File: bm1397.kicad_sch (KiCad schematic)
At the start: 68 parts, among them IC1 BM1397_mode1, J3 Conn_01x05, U2 LN1134A182MR-G, U3 SN74LVC1T45DBVR, U4 SGM2036-ADJYN5G/TR, U5 SN74LVC1T45DBVR, U6 SN74LVC1T45DBVR, U8 SN74LVC1T45DBVR, X1 OT322525MJBA4SL

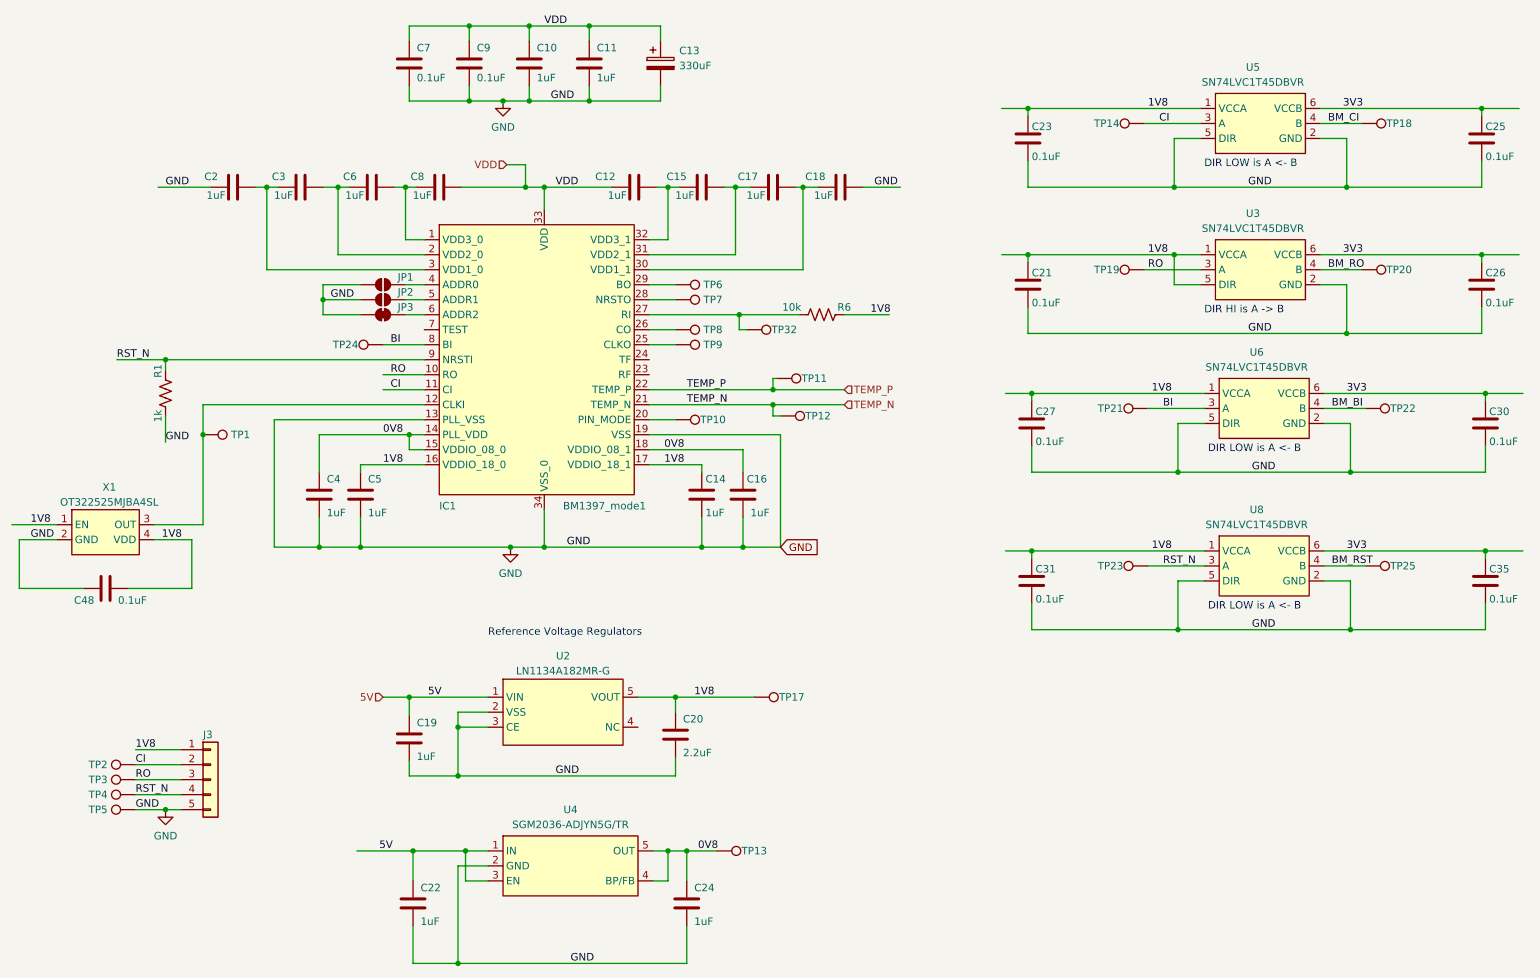
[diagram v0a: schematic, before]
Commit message: cleanup level shifters. LCRC inductor for buck
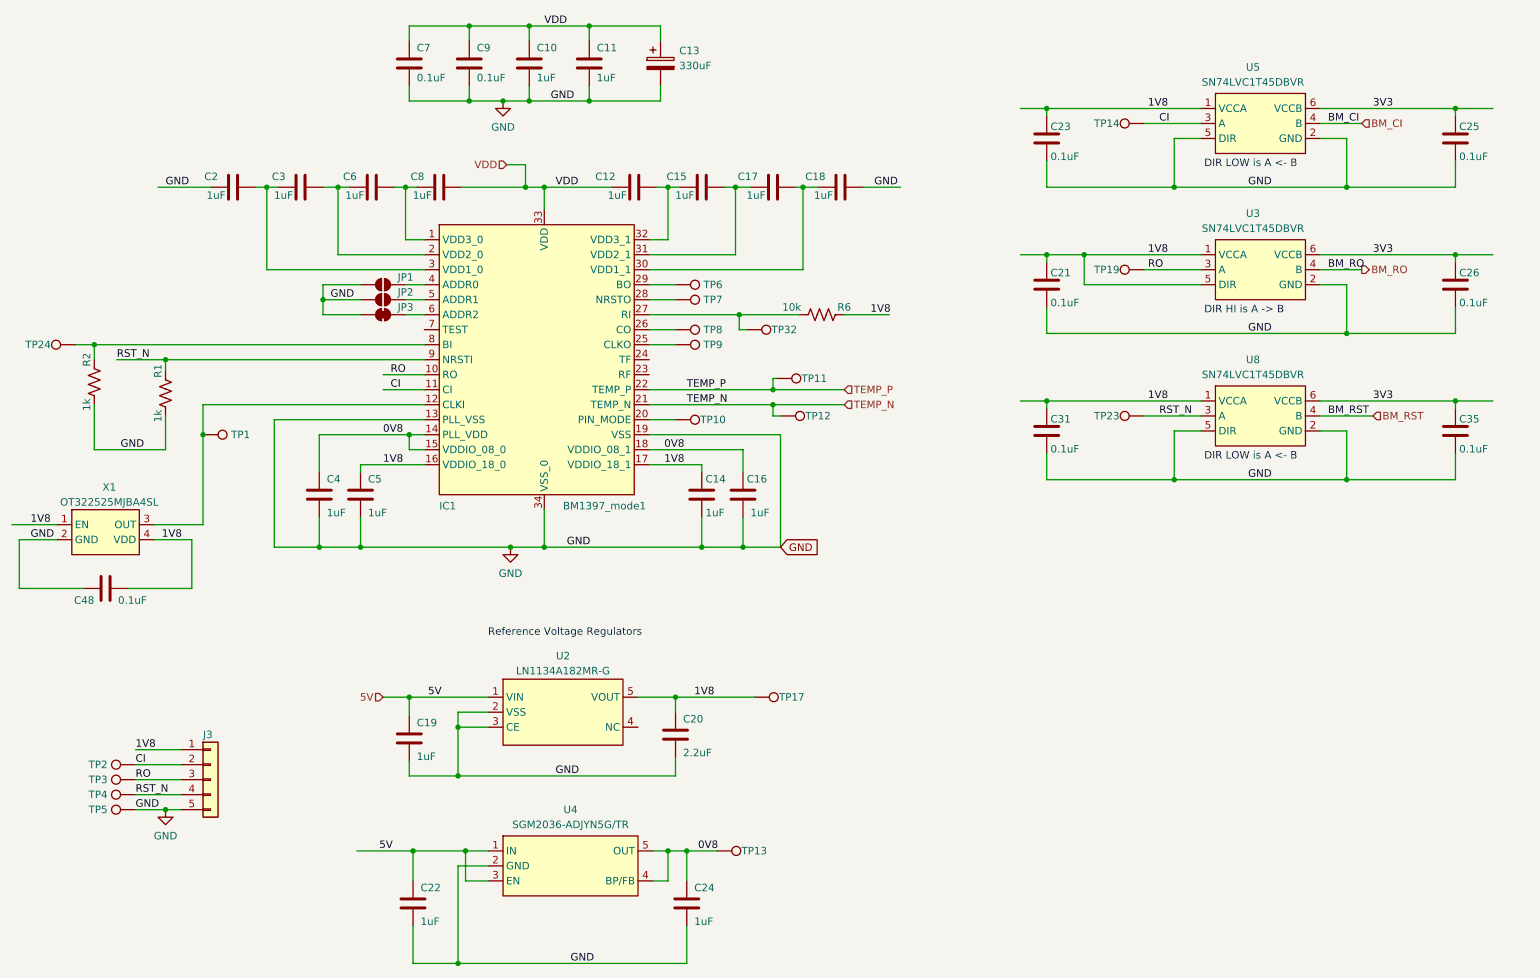
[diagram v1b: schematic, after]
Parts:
- removed C27, C30: 311-3342-1-ND, Capacitor_SMD:C_0402_1005Metric, symbol Device:C
- removed TP18, TP20, TP21, TP22, TP25: TestPoint, TestPoint:TestPoint_Pad_D1.5mm, symbol Connector:TestPoint
- removed U6: SN74LVC1T45DBVR, lcsc:SOT-23-6_L2.9-W1.6-P0.95-LS2.8-BR, symbol lcsc:SN74LVC1T45DBVR
- added R2: 1k, Resistor_SMD:R_0402_1005Metric, symbol Device:R_US
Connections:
- net GND: now also R2.1
- net BI: no longer names the net of IC1.8 (BI), TP24.1
- net BI: now also R2.2
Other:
- moved on the sheet: C21, C23, C25, C26, C31, C35, TP23, TP24, U8

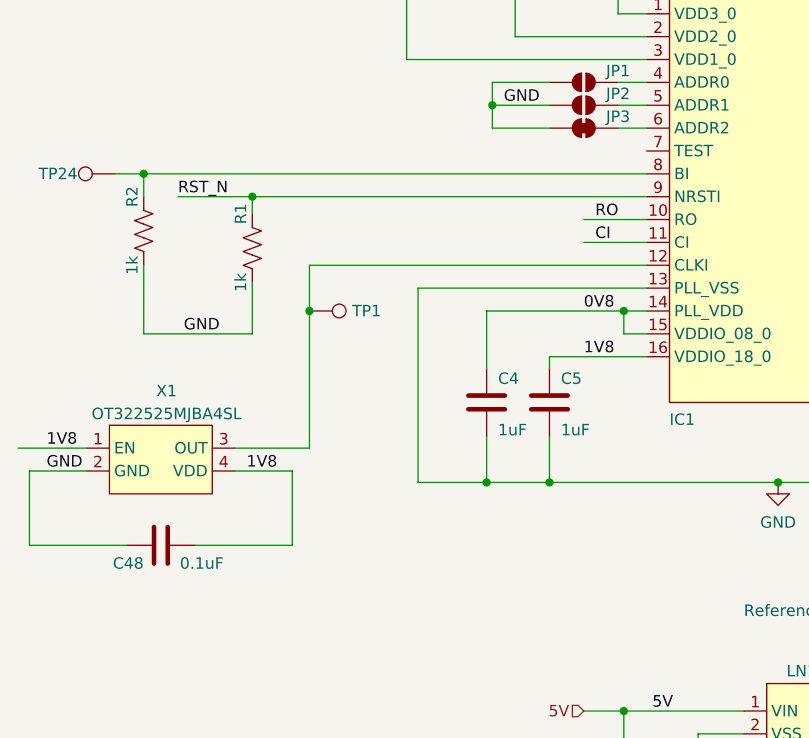
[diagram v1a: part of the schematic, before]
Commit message: fully removed BI (and pulled down at the BM1397)
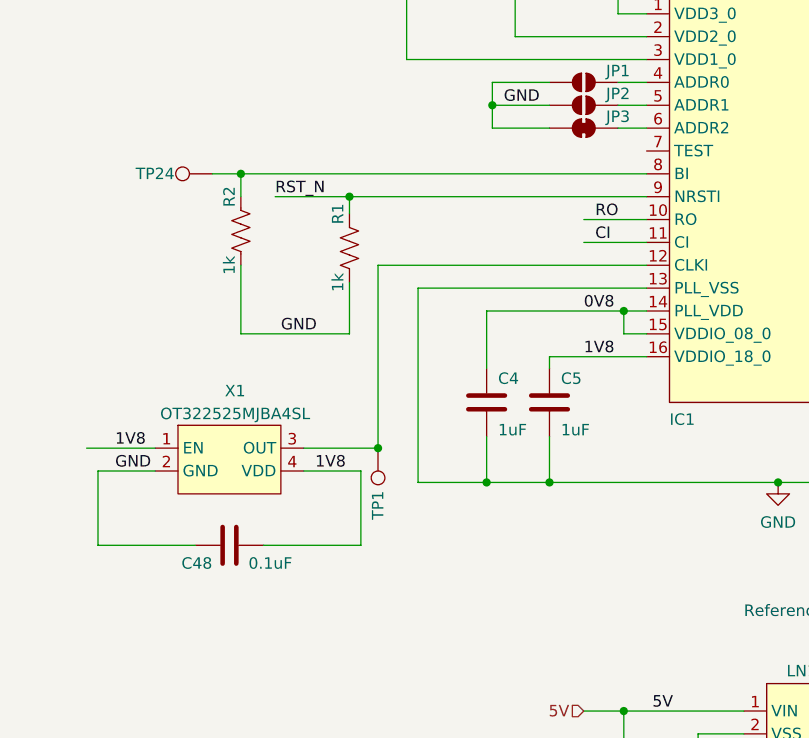
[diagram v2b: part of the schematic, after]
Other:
- moved on the sheet: C48, R1, R2, TP1, TP24, X1

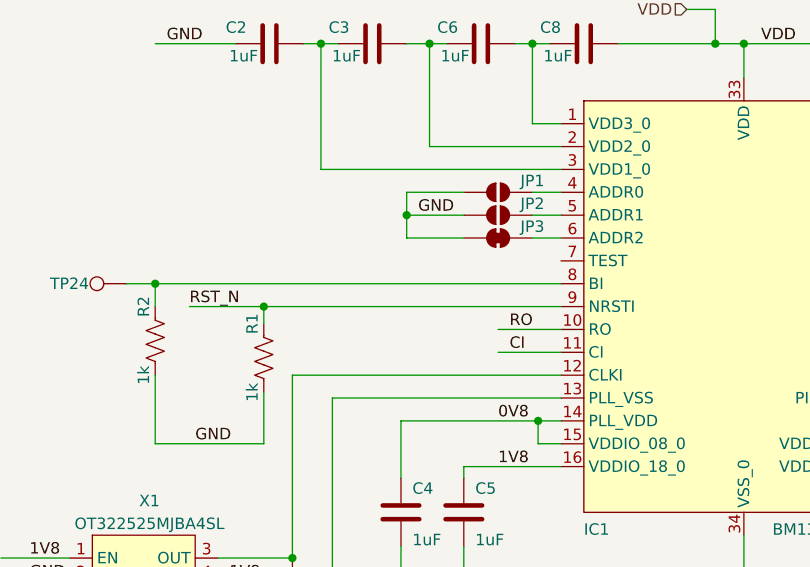
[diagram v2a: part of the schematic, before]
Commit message: adding 3D models. lots of placement. a little routing started
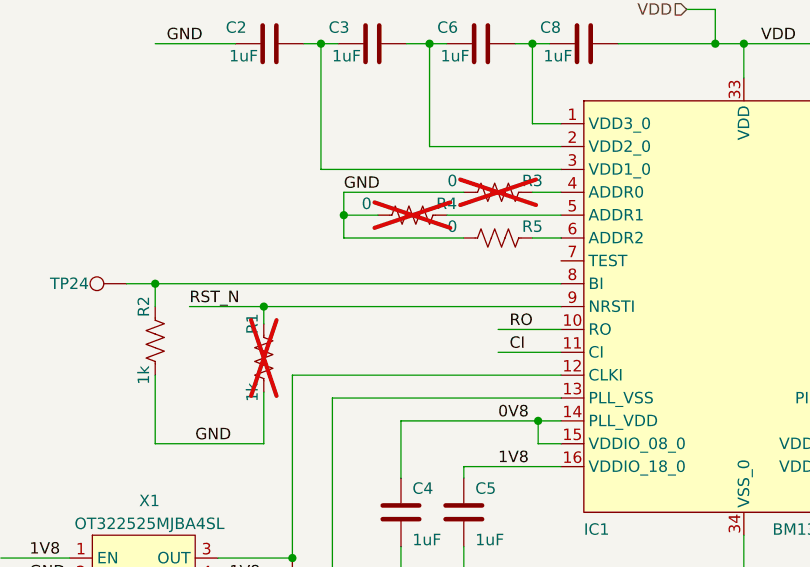
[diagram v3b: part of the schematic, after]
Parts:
- removed JP1, JP2: SolderJumper_2_Open, Jumper:SolderJumper-2_P1.3mm_Open_RoundedPad1.0x1.5mm, symbol Jumper:SolderJumper_2_Open
- removed JP3: SolderJumper_2_Bridged, Jumper:SolderJumper-2_P1.3mm_Bridged2Bar_RoundedPad1.0x1.5mm, symbol Jumper:SolderJumper_2_Bridged
- added R3, R4, R5: 0, Resistor_SMD:R_0402_1005Metric, symbol Device:R_US
- R1: now not fitted
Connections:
- net GND: now also R3.1, R4.1, R5.1
- net at IC1.4 (ADDR0): now also R3.2
- net at IC1.5 (ADDR1): now also R4.2
- net at IC1.6 (ADDR2): now also R5.2

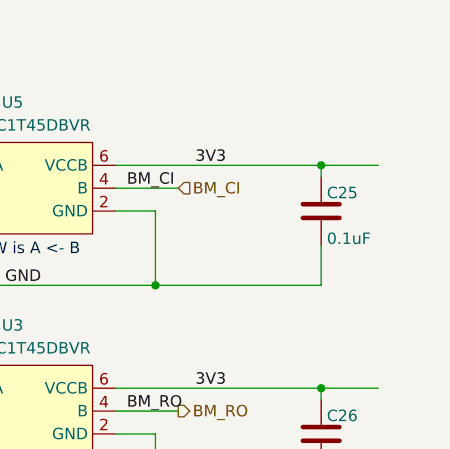
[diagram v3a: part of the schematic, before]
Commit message: pretty much all the signals are routed
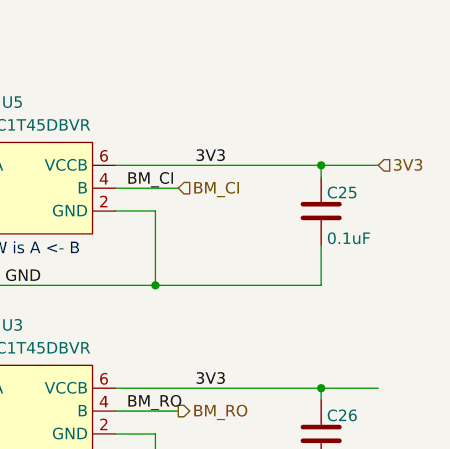
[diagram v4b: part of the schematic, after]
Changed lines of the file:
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@@
+    (effects (font (size 1.27 1.27)) (justify left))
+  )
+  (hierarchical_label "3V3" (shape input) (at 266.7 42.545 0) (fields_autoplaced)
     (effects (font (size 1.27 1.27)) (justify left))
   )

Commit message: finished routing
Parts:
- removed TP2, TP3, TP4: TestPoint, TestPoint:TestPoint_Pad_D1.5mm, symbol Connector:TestPoint
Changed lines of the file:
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@@
-    )
-  )
-  (symbol (lib_id "Connector:TestPoint") (at 36.83 153.67 90) (mirror x) (unit 1)
-    (in_bom yes) (on_board yes) (dnp no)
-    (property "Reference" "TP2" (at 30.48 153.67 90)
-      (effects (font (size 1.27 1.27)))
-    )
-    (property "Value" "TestPoint" (at 31.115 154.9399 90)
-      (effects (font (size 1.27 1.27)) (justify left) hide)
-    )
-    (property "Footprint" "TestPoint:TestPoint_Pad_D1.5mm" (at 36.83 158.75 0)
-      (effects (font (size 1.27 1.27)) hide)
-    )
-    (property "Datasheet" "~" (at 36.83 158.75 0)
-      (effects (font (size 1.27 1.27)) hide)
-    )
-    (property "DNP" "T" (at 36.83 153.67 0)
-      (effects (font (size 1.27 1.27)) hide)
-    )
-    (pin "1")
-    (instances
-      (project "Hashat"
-        (path "/00740941-7ad8-466a-a267-188591e2b5c4/5aa25910-cf6c-433c-86f8-40d28be84b47"
-          (reference "TP2") (unit 1)
-        )
-      )
-      (project "bitaxeMax"
-        (path "/e63e39d7-6ac0-4ffd-8aa3-1841a4541b55/4cf9c075-d009-4c35-9949-adda70ae20c7"
-          (reference "TP2") (unit 1)
-        )
-      )
     )
   )
@@
     )
   )
-  (symbol (lib_id "Connector:TestPoint") (at 36.83 158.75 90) (mirror x) (unit 1)
-    (in_bom yes) (on_board yes) (dnp no)
-    (property "Reference" "TP4" (at 30.48 158.75 90)
-      (effects (font (size 1.27 1.27)))
-    )
-    (property "Value" "TestPoint" (at 31.115 160.0199 90)
-      (effects (font (size 1.27 1.27)) (justify left) hide)
-    )
-    (property "Footprint" "TestPoint:TestPoint_Pad_D1.5mm" (at 36.83 163.83 0)
-      (effects (font (size 1.27 1.27)) hide)
-    )
-    (property "Datasheet" "~" (at 36.83 163.83 0)
-      (effects (font (size 1.27 1.27)) hide)
-    )
-    (property "DNP" "T" (at 36.83 158.75 0)
-      (effects (font (size 1.27 1.27)) hide)
-    )
-    (pin "1")
-    (instances
-      (project "Hashat"
-        (path "/00740941-7ad8-466a-a267-188591e2b5c4/5aa25910-cf6c-433c-86f8-40d28be84b47"
-          (reference "TP4") (unit 1)
-        )
-      )
-      (project "bitaxeMax"
-        (path "/e63e39d7-6ac0-4ffd-8aa3-1841a4541b55/4cf9c075-d009-4c35-9949-adda70ae20c7"
-          (reference "TP4") (unit 1)
-        )
-      )
-    )
-  )
   (symbol (lib_id "Device:R_US") (at 78.74 72.39 90) (unit 1)
     (in_bom yes) (on_board yes) (dnp yes)
@@
         )
       )
-    )
-  )
-  (symbol (lib_id "Connector:TestPoint") (at 36.83 156.21 90) (unit 1)
-    (in_bom yes) (on_board yes) (dnp no)
-    (property "Reference" "TP3" (at 30.48 156.21 90)
-      (effects (font (size 1.27 1.27)))
-    )
-    (property "Value" "TestPoint" (at 31.115 154.9401 90)
-      (effects (font (size 1.27 1.27)) (justify left) hide)
-    )
-    (property "Footprint" "TestPoint:TestPoint_Pad_D1.5mm" (at 36.83 151.13 0)
-      (effects (font (size 1.27 1.27)) hide)
-    )
-    (property "Datasheet" "~" (at 36.83 151.13 0)
-      (effects (font (size 1.27 1.27)) hide)
-    )
-    (property "DNP" "T" (at 36.83 156.21 0)
-      (effects (font (size 1.27 1.27)) hide)
-    )
-    (pin "1")
-    (instances
-      (project "Hashat"
-        (path "/00740941-7ad8-466a-a267-188591e2b5c4/5aa25910-cf6c-433c-86f8-40d28be84b47"
-          (reference "TP3") (unit 1)
-        )
-      )
-      (project "bitaxeMax"
-        (path "/e63e39d7-6ac0-4ffd-8aa3-1841a4541b55/4cf9c075-d009-4c35-9949-adda70ae20c7"
-          (reference "TP3") (unit 1)
-        )
-      )
